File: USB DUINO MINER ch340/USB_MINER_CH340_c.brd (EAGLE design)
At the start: 37.8 x 22.9 mm, 16 parts, among them J2 USB_A_PTH_MALE, U1 ATMEGA328P_TQFP, U2 CH340G, Y1 16MHZ, Y2 12MHz

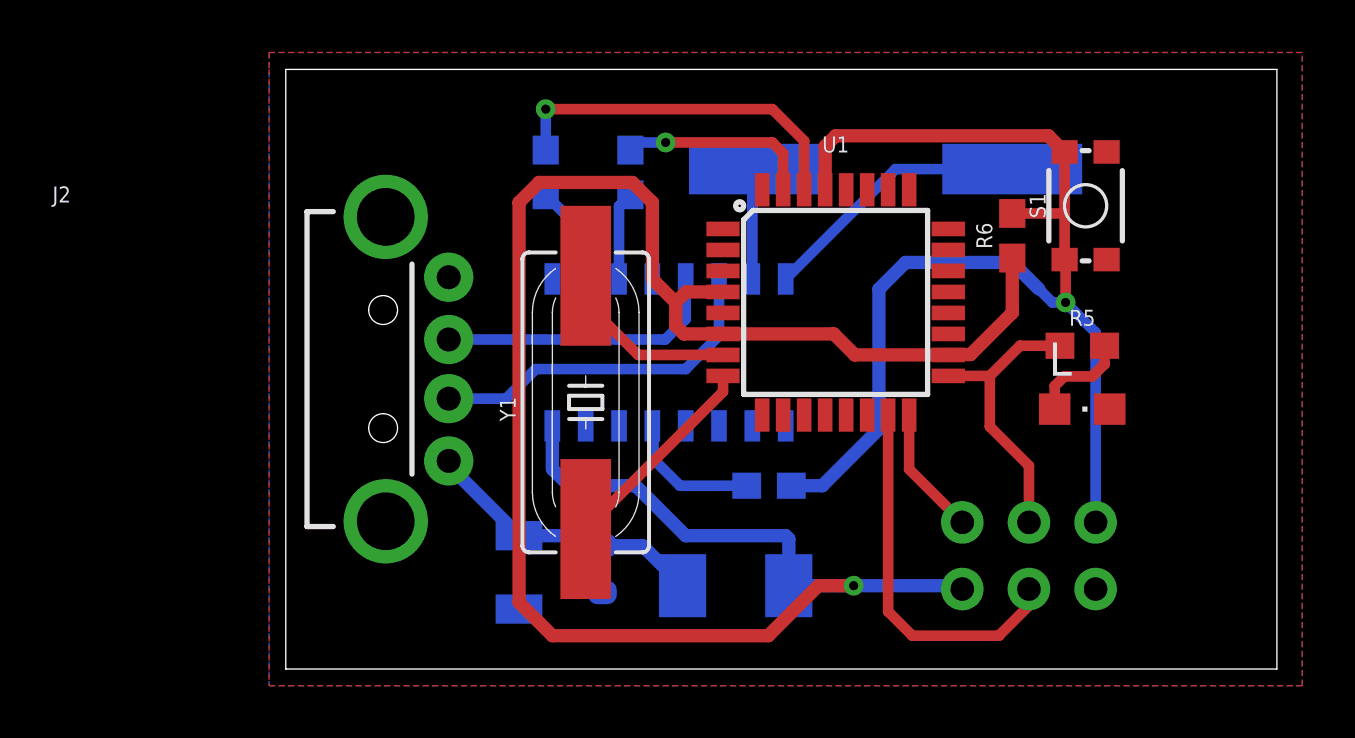
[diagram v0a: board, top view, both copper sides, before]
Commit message: update part
ubah part dengan ukuran 0603 menjadi 0805
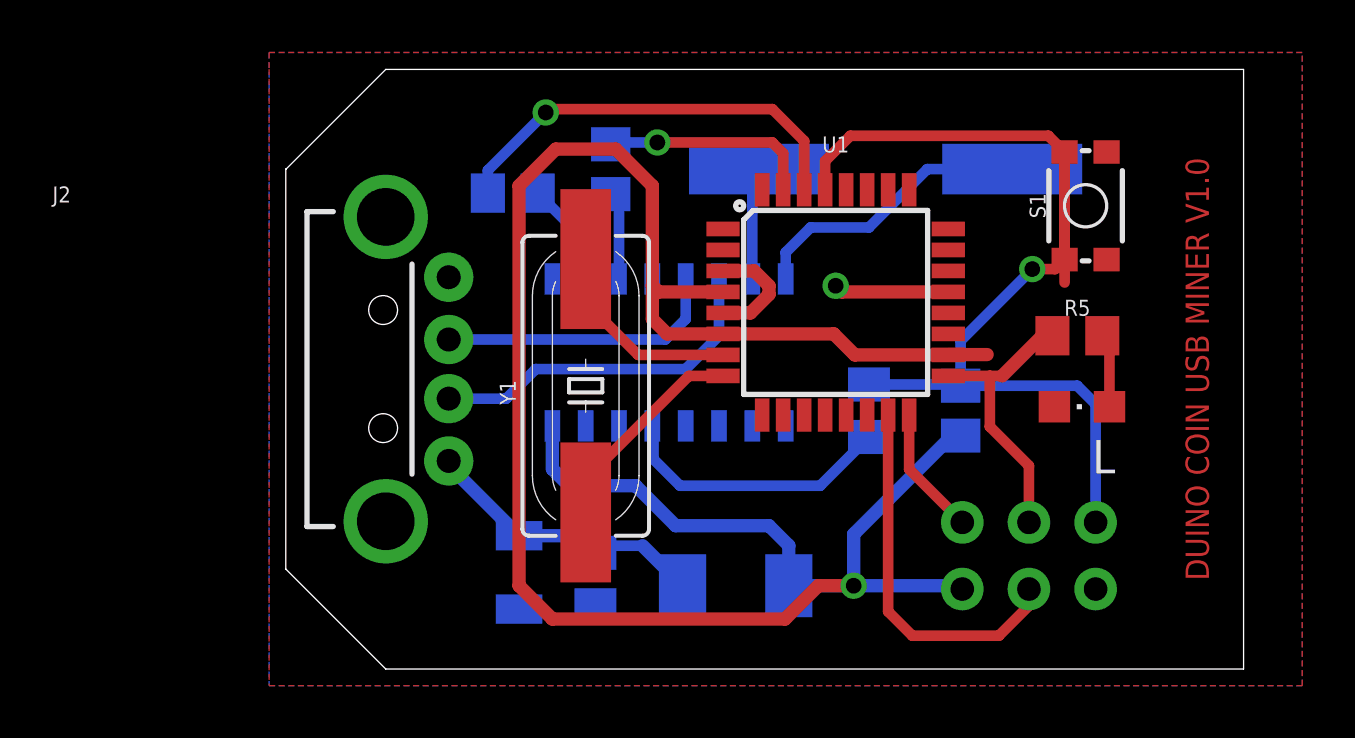
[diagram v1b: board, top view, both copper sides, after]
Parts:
- removed C1: 100nF, SparkFun-Capacitors:0603
- added C6: 100nF, rcl:C0805K
- C3: device Condensatori:C0603-ROUND -> rcl:C0805K
- R3, R4, R5, R6: device SparkFun-Resistors:0603 -> rcl:R0805
- moved C3 11.8 mm to (22.2, 9.84)
- moved R6 6.95 mm to (25.7, 9.85), flipped to the bottom
- moved R4 1.48 mm to (8.65, 18.1), turned to 0 degrees
- moved R3 0.76 mm to (12.4, 19.0)
- moved Y1 0.63 mm to (11.4, 10.8)
- moved R5 0.42 mm to (30.2, 12.7)
- moved L 0.09 mm to (30.3, 9.99), turned to 90 degrees
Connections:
- net COM: now also C6.2; no longer C3.2
- net N$14: now also C3.2; no longer C1.2
- net RESET: now also C3.1; no longer C1.1
- net VUSB: now also C6.1; no longer C3.1
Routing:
- net COM: track 0.00 -> 8.75 mm, vias 0 -> 1
- net +5V: track 78.3 -> 84.4 mm
- net N$14: track 5.26 -> 10.7 mm
- net RESET: track 45.6 -> 40.4 mm
- net N$13: track 13.8 -> 16.3 mm
- net N$7: track 4.11 -> 2.96 mm
- net N$12: track 7.51 -> 8.16 mm
- net N$3: track 7.08 -> 7.71 mm
- net N$2: track 10.4 -> 11.0 mm
- net VUSB: track 11.0 -> 11.5 mm
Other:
- board size 37.8 x 22.9 mm -> 36.5 x 22.9 mm
- board text added: "DUINO COIN USB MINER V1.0"
